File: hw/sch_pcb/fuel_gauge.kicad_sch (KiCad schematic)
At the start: 37 parts, among them Q2 AO3401A, Q3 AON7544, Q4 AON7544, U3 BQ40z50-R2

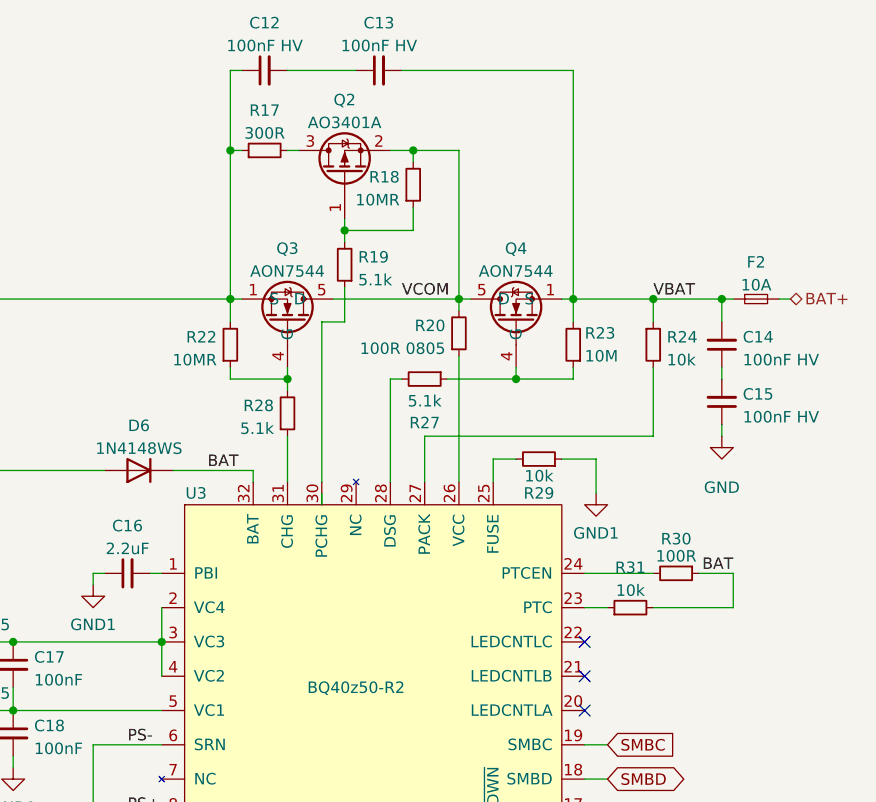
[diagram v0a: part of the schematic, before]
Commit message: Initial work on battery charging.
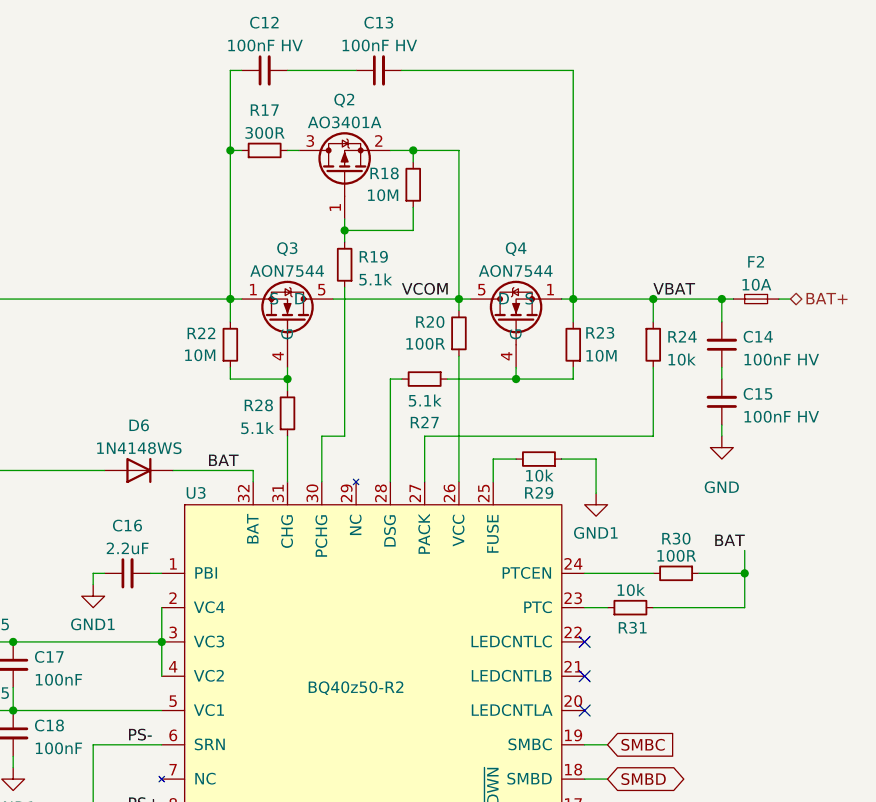
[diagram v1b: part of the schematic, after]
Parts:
- R18, R22: value 10MR -> 10M
- R20: value 100R 0805 -> 100R
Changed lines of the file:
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@@
 	)
 	(junction
+		(at 163.83 96.52)
+		(diameter 0)
+		(color 0 0 0 0)
+	)
+	(junction
 		(at 99.06 104.14)
 		(diameter 0)
@@
 	(wire
 		(pts
+			(xy 163.83 93.98) (xy 163.83 96.52)
+		)
+		(stroke
+			(width 0)
+			(type default)
+		)
+	)
+	(wire
+		(pts
 			(xy 109.22 85.09) (xy 109.22 86.36)
 		)
@@
 	(wire
 		(pts
-			(xy 153.67 100.33) (xy 162.56 100.33)
+			(xy 153.67 100.33) (xy 163.83 100.33)
 		)
 		(stroke
@@
 	(wire
 		(pts
-			(xy 119.38 64.77) (xy 119.38 68.58)
+			(xy 119.38 64.77) (xy 119.38 81.28)
 		)
 		(stroke
@@
 	(wire
 		(pts
+			(xy 163.83 96.52) (xy 158.75 96.52)
+		)
+		(stroke
+			(width 0)
+			(type default)
+		)
+	)
+	(wire
+		(pts
 			(xy 116.84 133.35) (xy 116.84 140.97)
 		)
@@
 	(wire
 		(pts
-			(xy 116.84 68.58) (xy 119.38 68.58)
+			(xy 116.84 81.28) (xy 119.38 81.28)
 		)
 		(stroke
@@
 	(wire
 		(pts
-			(xy 162.56 96.52) (xy 158.75 96.52)
-		)
-		(stroke
-			(width 0)
-			(type default)
-		)
-	)
-	(wire
-		(pts
 			(xy 123.19 152.4) (xy 123.19 151.13)
 		)
@@
 	(wire
 		(pts
-			(xy 116.84 87.63) (xy 116.84 88.9)
-		)
-		(stroke
-			(width 0)
-			(type default)
-		)
-	)
-	(wire
-		(pts
 			(xy 120.65 133.35) (xy 120.65 134.62)
 		)
@@
 	(wire
 		(pts
-			(xy 162.56 100.33) (xy 162.56 96.52)
-		)
-		(stroke
-			(width 0)
-			(type default)
-		)
-	)
-	(wire
-		(pts
 			(xy 135.89 139.7) (xy 135.89 140.97)
 		)
@@
 	(wire
 		(pts
-			(xy 116.84 68.58) (xy 116.84 86.36)
+			(xy 116.84 81.28) (xy 116.84 86.36)
 		)
 		(stroke
@@
 	(wire
 		(pts
+			(xy 163.83 96.52) (xy 163.83 100.33)
+		)
+		(stroke
+			(width 0)
+			(type default)
+		)
+	)
+	(wire
+		(pts
 			(xy 128.27 81.28) (xy 128.27 86.36)
 		)
@@
 	)
 	(label "BAT"
-		(at 162.56 96.52 180)
+		(at 163.83 93.98 180)
 		(fields_autoplaced yes)
 		(effects
@@
 		(fields_autoplaced yes)
 		(property "Reference" "R22"
-			(at 105.1815 70.2853 0)
+			(at 105.1814 69.9078 0)
 			(effects
 				(font
@@
 			)
 		)
-		(property "Value" "10MR"
-			(at 105.1815 72.8222 0)
+		(property "Value" "10M"
+			(at 105.1814 72.3321 0)
 			(effects
 				(font
@@
 		(on_board yes)
 		(dnp no)
-		(fields_autoplaced yes)
 		(property "Reference" "R31"
-			(at 151.13 95.8936 90)
+			(at 151.384 102.616 90)
 			(effects
 				(font
@@
 		(fields_autoplaced yes)
 		(property "Reference" "R20"
-			(at 130.5815 69.0153 0)
+			(at 130.5815 68.6378 0)
 			(effects
 				(font
@@
 			)
 		)
-		(property "Value" "100R 0805"
-			(at 130.5815 71.5522 0)
+		(property "Value" "100R"
+			(at 130.5815 71.0621 0)
 			(effects
 				(font
@@
 		(fields_autoplaced yes)
 		(property "Reference" "R18"
-			(at 125.5015 52.5053 0)
+			(at 125.5014 52.1278 0)
 			(effects
 				(font
@@
 			)
 		)
-		(property "Value" "10MR"
-			(at 125.5015 55.0422 0)
+		(property "Value" "10M"
+			(at 125.5014 54.5521 0)
 			(effects
 				(font

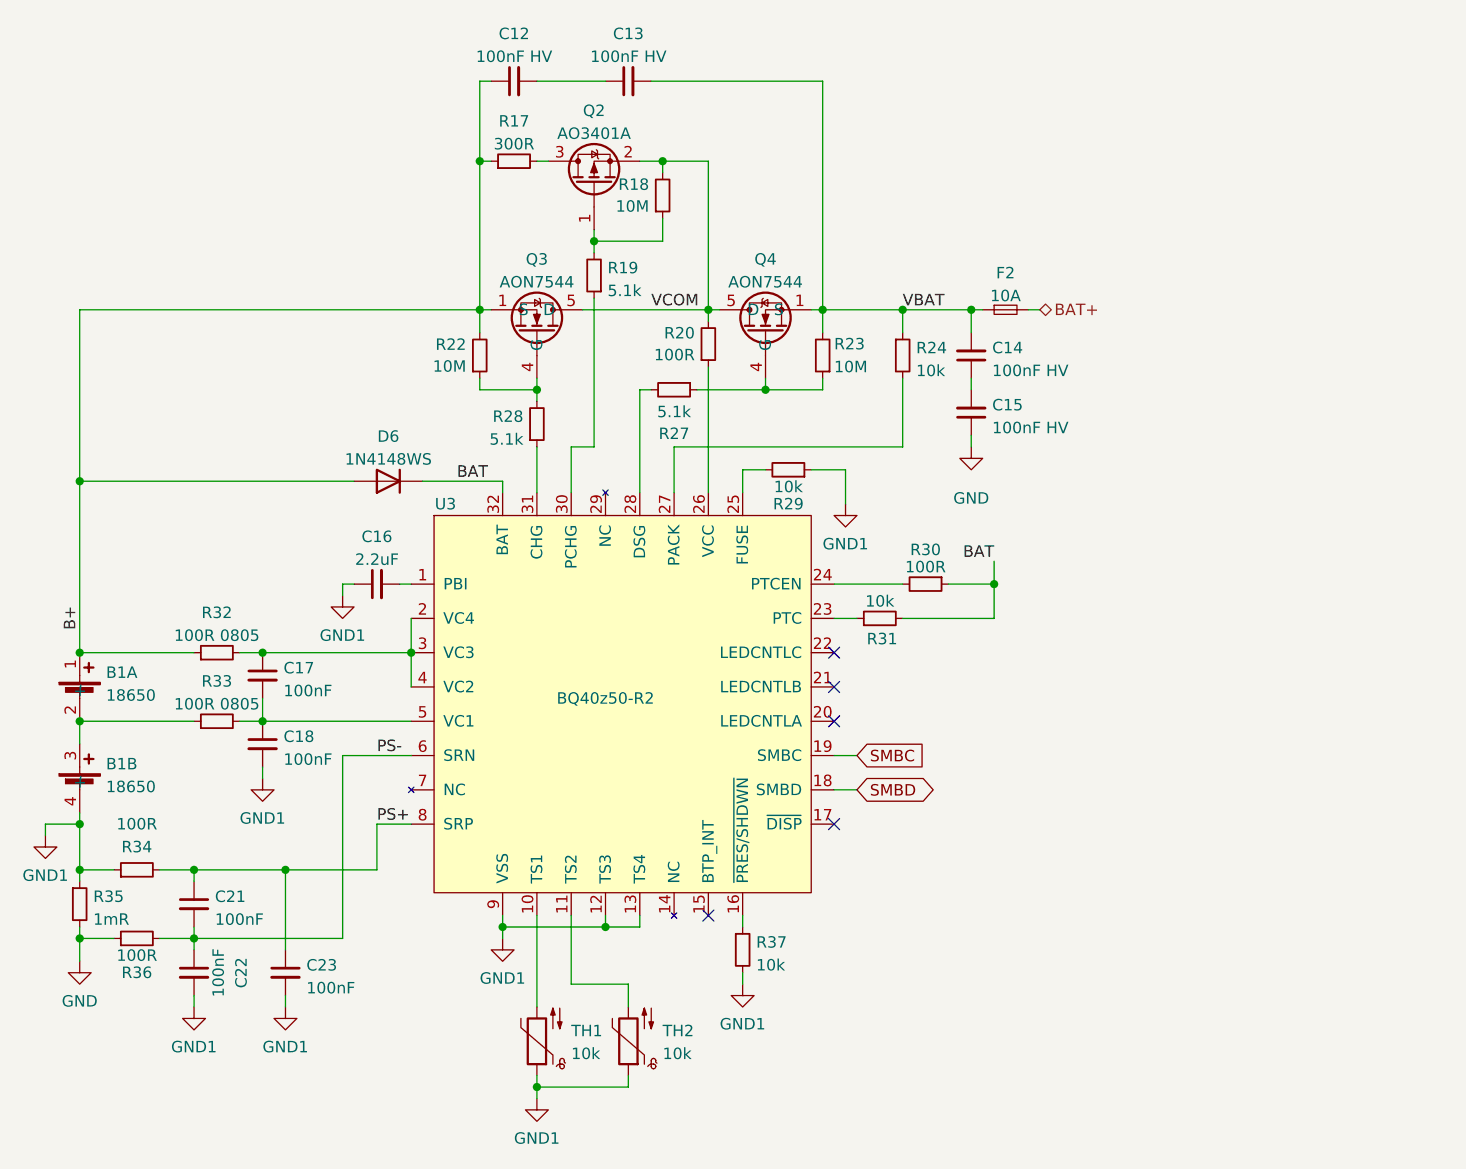
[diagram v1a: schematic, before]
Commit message: Fuel gauge schematics work done.
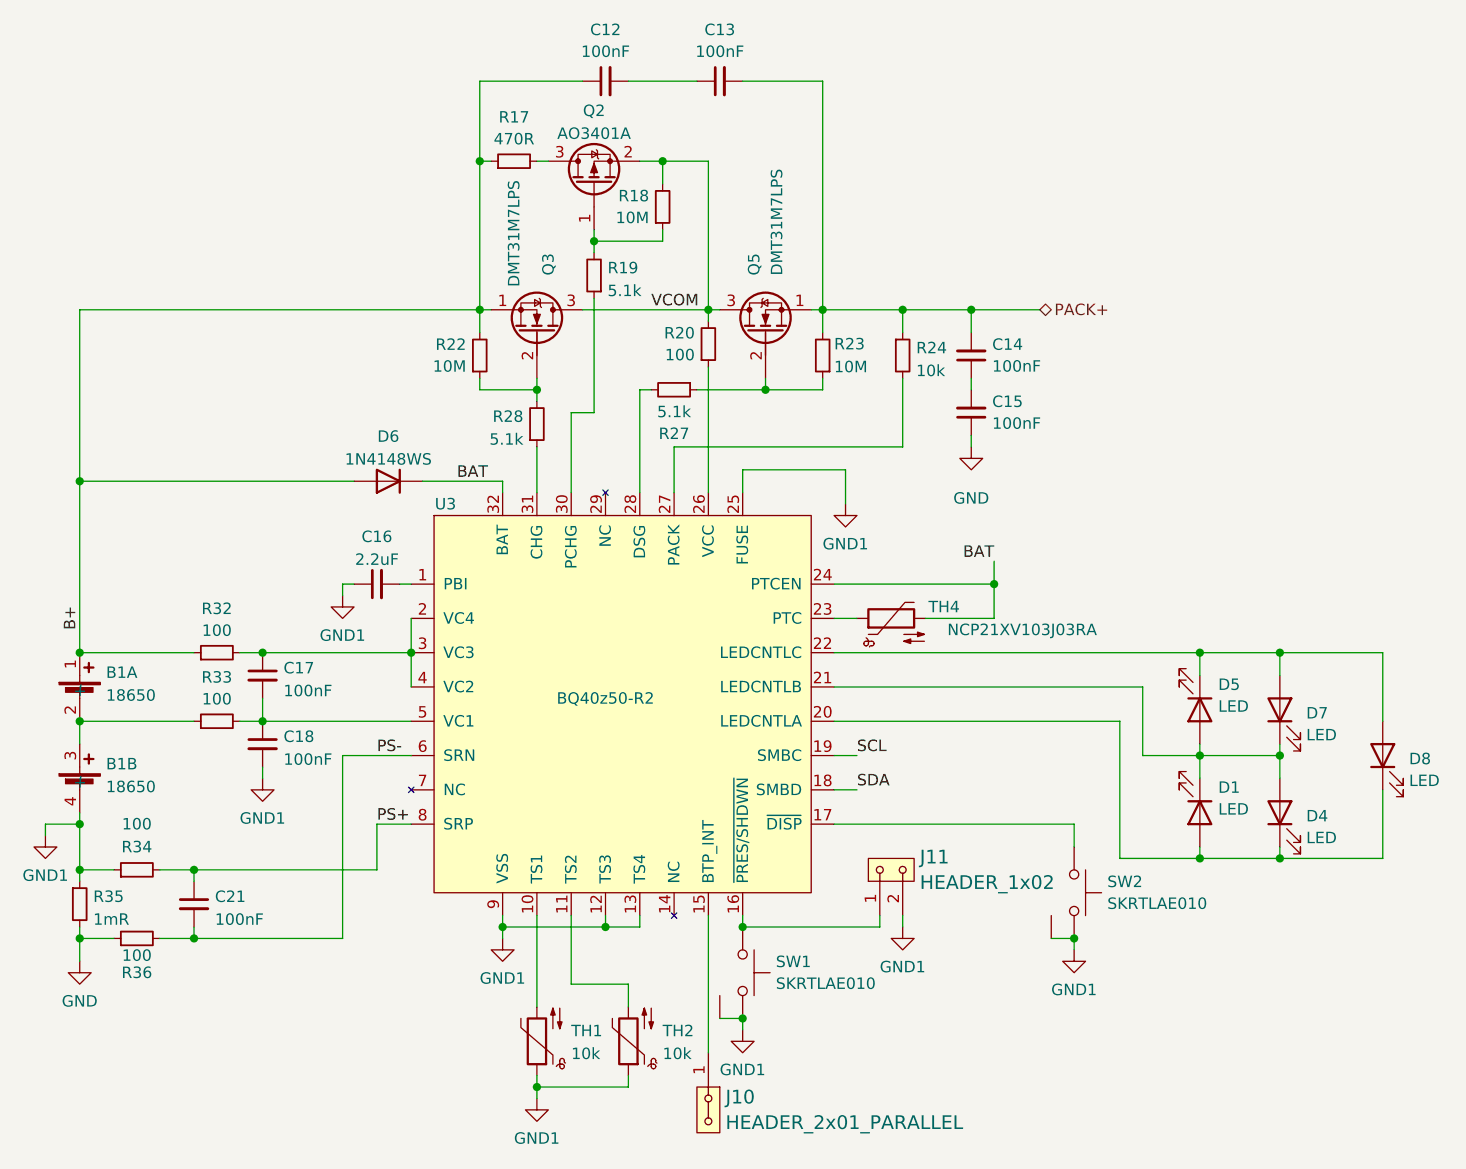
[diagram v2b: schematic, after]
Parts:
- removed C22, C23: 100nF, Capacitor_SMD:C_0402_1005Metric, symbol Device:C_Small
- removed F2: 10A, Fuse:Fuse_1206_3216Metric, symbol Device:Fuse_Small
- removed Q3, Q4: AON7544, Package_DFN_FET:DFN-8-FET_3x3mm_P0.65mm, symbol Transistor_FET_DFN:AON7544
- removed R29, R31, R37: 10k, Resistor_SMD:R_0402_1005Metric, symbol Device:R_Small
- removed R30: 100R, Resistor_SMD:R_0402_1005Metric, symbol Device:R_Small
- added D1, D4, D5, D7, D8: LED, symbol Device:LED
- added J10: HEADER_2x01_PARALLEL, symbol MLAB_HEADER:HEADER_2x01_PARALLEL
- added J11: HEADER_1x02, symbol MLAB_HEADER:HEADER_1x02
- added Q3, Q5: DMT31M7LPS, Mlab_IO:PowerDI5060-8, symbol Device:Q_NMOS_SGD
- added SW1, SW2: SKRTLAE010, Mlab_SW:SKRT, symbol MLAB_SW:SW_Push_shield
- added TH4: NCP21XV103J03RA, Resistor_SMD:R_0805_2012Metric, symbol Device:Thermistor_NTC
- C12, C13, C14, C15: value 100nF HV -> 100nF
- R17: value 300R -> 470R
- R20, R34, R36: value 100R -> 100
- R32, R33: value 100R 0805 -> 100
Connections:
- net B+: now also Q3.1 (S)
- net BAT: now also U3.24 (PTCEN), TH4.2
- net GND1: now also U3.25 (FUSE), J11.2, SW1.2, SW1.GND (SHIELD), SW2.2, SW2.GND (SHIELD)
- net VCOM: now also Q3.3 (D), Q5.3 (D)
- net at R22.1, R28.2: now also Q3.2 (G)
- net at U3.16 (~{PRES/SHDWN}): now also J11.1, SW1.1
- net at U3.15 (BTP_INT): now also J10.1, J10.2
- net at U3.17 (~{DISP}): now also SW2.1
- net at U3.20 (LEDCNTLA): now also D1.2 (A), D4.1 (K), D8.1 (K)
- net at U3.21 (LEDCNTLB): now also D1.1 (K), D4.2 (A), D5.2 (A), D7.1 (K)
- net at U3.22 (LEDCNTLC): now also D5.1 (K), D7.2 (A), D8.2 (A)
- net at U3.23 (PTC): now also TH4.1
- net at R23.1, R27.1: now also Q5.2 (G)
- net SMBC renamed SCL
- net SMBD renamed SDA
- net VBAT renamed PACK+
- net PACK+: now also Q5.1 (S)
- no-connect marks 5 -> 0
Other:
- moved on the sheet: C12, C13, R18

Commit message: Schematics work. PCB layout initial schematics import.
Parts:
- B1: footprint battery-holder-keystone:SMD-1048-dual-18650 -> Mlab_Batery:BAT_BK-18650-PC4_no_screws; UST_ID (none) -> 5c70984412875079b91f87e9
- D1, D4, D5, D7, D8: footprint (none) -> Mlab_D:LED_1206
- J10, J11: footprint (none) -> Mlab_Pin_Headers:Straight_1x02
- U3: footprint Package_Texas:VQFN-32-4.1x4.1-EP-1.4 -> Mlab_IO:Texas_RSM0032A_VQFN-32-4.1x4.1-EP-1.4
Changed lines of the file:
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@@
 			)
 		)
-		(property "Footprint" "Package_Texas:VQFN-32-4.1x4.1-EP-1.4"
+		(property "Footprint" "Mlab_IO:Texas_RSM0032A_VQFN-32-4.1x4.1-EP-1.4"
 			(at 120.65 109.22 0)
 			(effects
@@
 			)
 		)
-		(property "Footprint" ""
+		(property "Footprint" "Mlab_D:LED_1206"
 			(at 207.01 115.57 0)
 			(effects
@@
 			)
 		)
-		(property "Footprint" ""
+		(property "Footprint" "Mlab_Pin_Headers:Straight_1x02"
 			(at 151.13 128.27 0)
 			(effects
@@
 					(size 1.524 1.524)
 				)
+				(hide yes)
 			)
 		)
@@
 			)
 		)
-		(property "Footprint" "battery-holder-keystone:SMD-1048-dual-18650"
+		(property "Footprint" "Mlab_Batery:BAT_BK-18650-PC4_no_screws"
 			(at 62.23 118.11 0)
 			(effects
@@
 		)
 		(property "Description" ""
+			(at 62.23 118.11 0)
+			(effects
+				(font
+					(size 1.27 1.27)
+				)
+				(hide yes)
+			)
+		)
+		(property "UST_ID" "5c70984412875079b91f87e9"
 			(at 62.23 118.11 0)
 			(effects
@@
 			)
 		)
-		(property "Footprint" "battery-holder-keystone:SMD-1048-dual-18650"
+		(property "Footprint" "Mlab_Batery:BAT_BK-18650-PC4_no_screws"
 			(at 62.23 107.95 0)
 			(effects
@@
 			)
 		)
+		(property "UST_ID" "5c70984412875079b91f87e9"
+			(at 62.23 107.95 0)
+			(effects
+				(font
+					(size 1.27 1.27)
+				)
+				(hide yes)
+			)
+		)
 		(pin "1"
 		)
@@
 			)
 		)
-		(property "Footprint" ""
+		(property "Footprint" "Mlab_D:LED_1206"
 			(at 195.58 121.92 0)
 			(effects
@@
 			)
 		)
-		(property "Footprint" ""
+		(property "Footprint" "Mlab_Pin_Headers:Straight_1x02"
 			(at 132.08 154.94 0)
 			(effects
@@
 					(size 1.524 1.524)
 				)
+				(hide yes)
 			)
 		)
@@
 			)
 		)
-		(property "Footprint" ""
+		(property "Footprint" "Mlab_D:LED_1206"
 			(at 186.69 121.92 0)
 			(effects
@@
 			)
 		)
-		(property "Footprint" ""
+		(property "Footprint" "Mlab_D:LED_1206"
 			(at 186.69 110.49 0)
 			(effects
@@
 			)
 		)
-		(property "Footprint" ""
+		(property "Footprint" "Mlab_D:LED_1206"
 			(at 195.58 110.49 0)
 			(effects
